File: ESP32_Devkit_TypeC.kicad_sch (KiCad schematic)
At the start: 57 parts, among them J1 USB_C_Receptacle_USB2.0, J2 Conn_01x19, J3 Conn_01x19, Q1 SS8050, Q2 SS8050, SW1 EN, SW2 BOOT, U1 MP2359, U2 CH340G, U3 ESP32-PICO-D4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

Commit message: Updated DC-DC convertor, fixed CH340G Vout
I changed switching regulator to MP2259, because MP2359 is not recommended for new designs and is therefore more futureproof.
Resistor values was also changed to lower the voltage from 3.5V to 3.33V.
I also changed USB-C type to TYPE-C-31-M-12, because I have it :) It also seems to be more popular and I saw many compatible clones on Aliexpress for example.
CH340G was set to operate with 5V signals, which isn't good for ESP, so I changed it. I also changed the part to CH340C to avoid using external crystal (which will be optional for CH340G compatibility).
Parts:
- J1: footprint Connector_USB:USB_C_Receptacle_Palconn_UTC16-G -> Connector_USB:USB_C_Receptacle_HRO_TYPE-C-31-M-12; LCSC C167321 -> C165948
- R5: value 49.9kR -> 56kR; LCSC C25897 -> C25796
- R6: value 15 kR -> 18 kR; LCSC C25756 -> C25762
- U1: value MP2359 -> MP2259; LCSC C14259 -> C82266
- U2: value CH340G -> CH340C; LCSC C14267 -> C84681
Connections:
- net +3V3: now also C5.2, C7.2, U2.16 (VCC), U2.4 (V3)
- net GND: now also C5.1; no longer C5.2
- net VBUS: no longer C7.2, U2.16 (VCC)
- no-connect marks 2 -> 9
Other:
- note added: "Populate only if CH340G is used!"
- moved on the sheet: C1, C10, C11, C2, C3, C4, C5, C7, C8, C9, D1, D2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

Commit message: Changed 4.7uF inductor part
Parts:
- L1: LCSC C86070 -> C90319
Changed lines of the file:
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@@
       (effects (font (size 1.27 1.27)) hide)
     )
-    (property "LCSC" "C86070" (id 4) (at 78.74 149.86 90)
+    (property "LCSC" " C90319" (id 4) (at 78.74 149.86 90)
       (effects (font (size 1.27 1.27)) hide)
     )

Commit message: Updated footprints, reconnected CH340C
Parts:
- J1: footprint Connector_USB:USB_C_Receptacle_HRO_TYPE-C-31-M-12 -> Moucha_Connectors:USBC_Receptacle_TYPE-C-31-M-12
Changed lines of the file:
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@@
     (property "Reference" "J1" (id 0) (at 37.0078 40.2082 0))
     (property "Value" "USB_C_Receptacle_USB2.0" (id 1) (at 37.0078 42.5196 0))
-    (property "Footprint" "Connector_USB:USB_C_Receptacle_HRO_TYPE-C-31-M-12" (id 2) (at 38.1 62.23 0)
+    (property "Footprint" "Moucha_Connectors:USBC_Receptacle_TYPE-C-31-M-12" (id 2) (at 38.1 62.23 0)
       (effects (font (size 1.27 1.27)) hide)
     )
@@
   (symbol (lib_id "power:+3V3") (at 83.82 33.02 0) (unit 1)
     (in_bom yes) (on_board yes)
-    (property "Reference" "#PWR?" (id 0) (at 83.82 36.83 0)
+    (property "Reference" "#PWR0130" (id 0) (at 83.82 36.83 0)
       (effects (font (size 1.27 1.27)) hide)
     )
@@
   (symbol (lib_id "power:GND") (at 69.85 41.91 0) (unit 1)
     (in_bom yes) (on_board yes)
-    (property "Reference" "#PWR?" (id 0) (at 69.85 48.26 0)
+    (property "Reference" "#PWR0106" (id 0) (at 69.85 48.26 0)
       (effects (font (size 1.27 1.27)) hide)
     )
@@
       (reference "#PWR0105") (unit 1) (value "GND") (footprint "")
     )
+    (path "/e89e4f7f-5566-4b18-a6b1-ab29876f8a10"
+      (reference "#PWR0106") (unit 1) (value "GND") (footprint "")
+    )
     (path "/00000000-0000-0000-0000-00005eb6312c"
       (reference "#PWR0107") (unit 1) (value "GND") (footprint "")
@@
     )
     (path "/81b97e70-46f3-4336-aebf-837d4cb8d978"
-      (reference "#PWR?") (unit 1) (value "+3V3") (footprint "")
-    )
-    (path "/e89e4f7f-5566-4b18-a6b1-ab29876f8a10"
-      (reference "#PWR?") (unit 1) (value "GND") (footprint "")
+      (reference "#PWR0130") (unit 1) (value "+3V3") (footprint "")
     )
     (path "/00000000-0000-0000-0000-00005f1a8ada"
@@
     )
     (path "/00000000-0000-0000-0000-00005eb3eb53"
-      (reference "J1") (unit 1) (value "USB_C_Receptacle_USB2.0") (footprint "Connector_USB:USB_C_Receptacle_HRO_TYPE-C-31-M-12")
+      (reference "J1") (unit 1) (value "USB_C_Receptacle_USB2.0") (footprint "Moucha_Connectors:USBC_Receptacle_TYPE-C-31-M-12")
     )
     (path "/00000000-0000-0000-0000-00005eca1541"

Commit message: Changed button type, DRC fixes
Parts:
- SW1, SW2: footprint Button_Switch_SMD:SW_Push_SPST_NO_Alps_SKRK -> Moucha_Primitives:SW_Push_1P1T_Vertical_3x4mm; LCSC C115357 -> C589212
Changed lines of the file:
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@@
     (property "Reference" "SW1" (id 0) (at 149.86 49.911 0))
     (property "Value" "EN" (id 1) (at 149.86 52.2224 0))
-    (property "Footprint" "Button_Switch_SMD:SW_Push_SPST_NO_Alps_SKRK" (id 2) (at 149.86 52.07 0)
+    (property "Footprint" "Moucha_Primitives:SW_Push_1P1T_Vertical_3x4mm" (id 2) (at 149.86 52.07 0)
       (effects (font (size 1.27 1.27)) hide)
     )
@@
       (effects (font (size 1.27 1.27)) hide)
     )
-    (property "LCSC" "C115357" (id 4) (at 149.86 57.15 0)
+    (property "LCSC" "C589212" (id 4) (at 149.86 57.15 0)
       (effects (font (size 1.27 1.27)) hide)
     )
@@
     (property "Reference" "SW2" (id 0) (at 149.86 70.231 0))
     (property "Value" "BOOT" (id 1) (at 149.86 72.5424 0))
-    (property "Footprint" "Button_Switch_SMD:SW_Push_SPST_NO_Alps_SKRK" (id 2) (at 149.86 72.39 0)
+    (property "Footprint" "Moucha_Primitives:SW_Push_1P1T_Vertical_3x4mm" (id 2) (at 149.86 72.39 0)
       (effects (font (size 1.27 1.27)) hide)
     )
@@
       (effects (font (size 1.27 1.27)) hide)
     )
-    (property "LCSC" "C115357" (id 4) (at 149.86 77.47 0)
+    (property "LCSC" "C589212" (id 4) (at 149.86 77.47 0)
       (effects (font (size 1.27 1.27)) hide)
     )
@@
     )
     (path "/00000000-0000-0000-0000-00005eca28f9"
-      (reference "SW1") (unit 1) (value "EN") (footprint "Button_Switch_SMD:SW_Push_SPST_NO_Alps_SKRK")
+      (reference "SW1") (unit 1) (value "EN") (footprint "Moucha_Primitives:SW_Push_1P1T_Vertical_3x4mm")
     )
     (path "/00000000-0000-0000-0000-00005eca6673"
-      (reference "SW2") (unit 1) (value "BOOT") (footprint "Button_Switch_SMD:SW_Push_SPST_NO_Alps_SKRK")
+      (reference "SW2") (unit 1) (value "BOOT") (footprint "Moucha_Primitives:SW_Push_1P1T_Vertical_3x4mm")
     )
     (path "/00000000-0000-0000-0000-00005eb3cfab"

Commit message: updated documentation
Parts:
- AE1, C10, C11, C9, H1, H2, I2, JP1: now left out of the parts list
- J1: footprint Moucha_Connectors:USBC_Receptacle_TYPE-C-31-M-12 -> Connector_USB:USB_C_Receptacle_HRO_TYPE-C-31-M-12
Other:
- moved on the sheet: AE1, C12, C13, C14, C15, C16, C17, C18, C19, C20, C21, C22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

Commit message: Fixed component rotation
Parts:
- L1: LCSC C90319 -> C90319
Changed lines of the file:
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@@
       (effects (font (size 1.27 1.27)) hide)
     )
-    (property "LCSC" " C90319" (id 4) (at 78.74 149.86 90)
+    (property "LCSC" "C90319" (id 4) (at 78.74 149.86 90)
       (effects (font (size 1.27 1.27)) hide)
     )

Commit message: Rev EB serial transciever bugfix, component upgrade
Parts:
- U3: footprint Package_ESP32:ESP32-Pico-D4 -> Package_ESP32:ESP32-Pico-D4-Handsolder
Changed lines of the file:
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@@
   (title_block
     (title "ESP32 DevKit Type C")
-    (date "2022-03-13")
-    (rev "F")
+    (date "2022-03-17")
+    (rev "EB")
   )
   (junction (at 60.96 99.06) (diameter 0) (color 0 0 0 0)
@@
     (stroke (width 0) (type default) (color 0 0 0 0))
   )
-  (polyline (pts (xy 50.8 77.47) (xy 80.01 77.47))
+  (polyline (pts (xy 50.8 80.01) (xy 80.01 77.47))
     (stroke (width 0) (type default) (color 0 0 0 0))
   )
@@
     (stroke (width 0) (type default) (color 0 0 0 0))
   )
-  (polyline (pts (xy 50.8 100.33) (xy 50.8 77.47))
+  (polyline (pts (xy 50.8 100.33) (xy 50.8 80.01))
     (stroke (width 0) (type default) (color 0 0 0 0))
   )
@@
     (property "Reference" "U3" (id 0) (at 208.28 78.74 0))
     (property "Value" "ESP32-PICO-D4" (id 1) (at 234.95 78.74 0))
-    (property "Footprint" "Package_ESP32:ESP32-Pico-D4" (id 2) (at 222.25 161.29 0)
+    (property "Footprint" "Package_ESP32:ESP32-Pico-D4-Handsolder" (id 2) (at 222.25 161.29 0)
       (effects (font (size 1.27 1.27)) hide)
     )
@@
     )
     (path "/00000000-0000-0000-0000-00005eb3c833"
-      (reference "U3") (unit 1) (value "ESP32-PICO-D4") (footprint "Package_ESP32:ESP32-Pico-D4")
+      (reference "U3") (unit 1) (value "ESP32-PICO-D4") (footprint "Package_ESP32:ESP32-Pico-D4-Handsolder")
     )
     (path "/00000000-0000-0000-0000-00005eb3dda3"

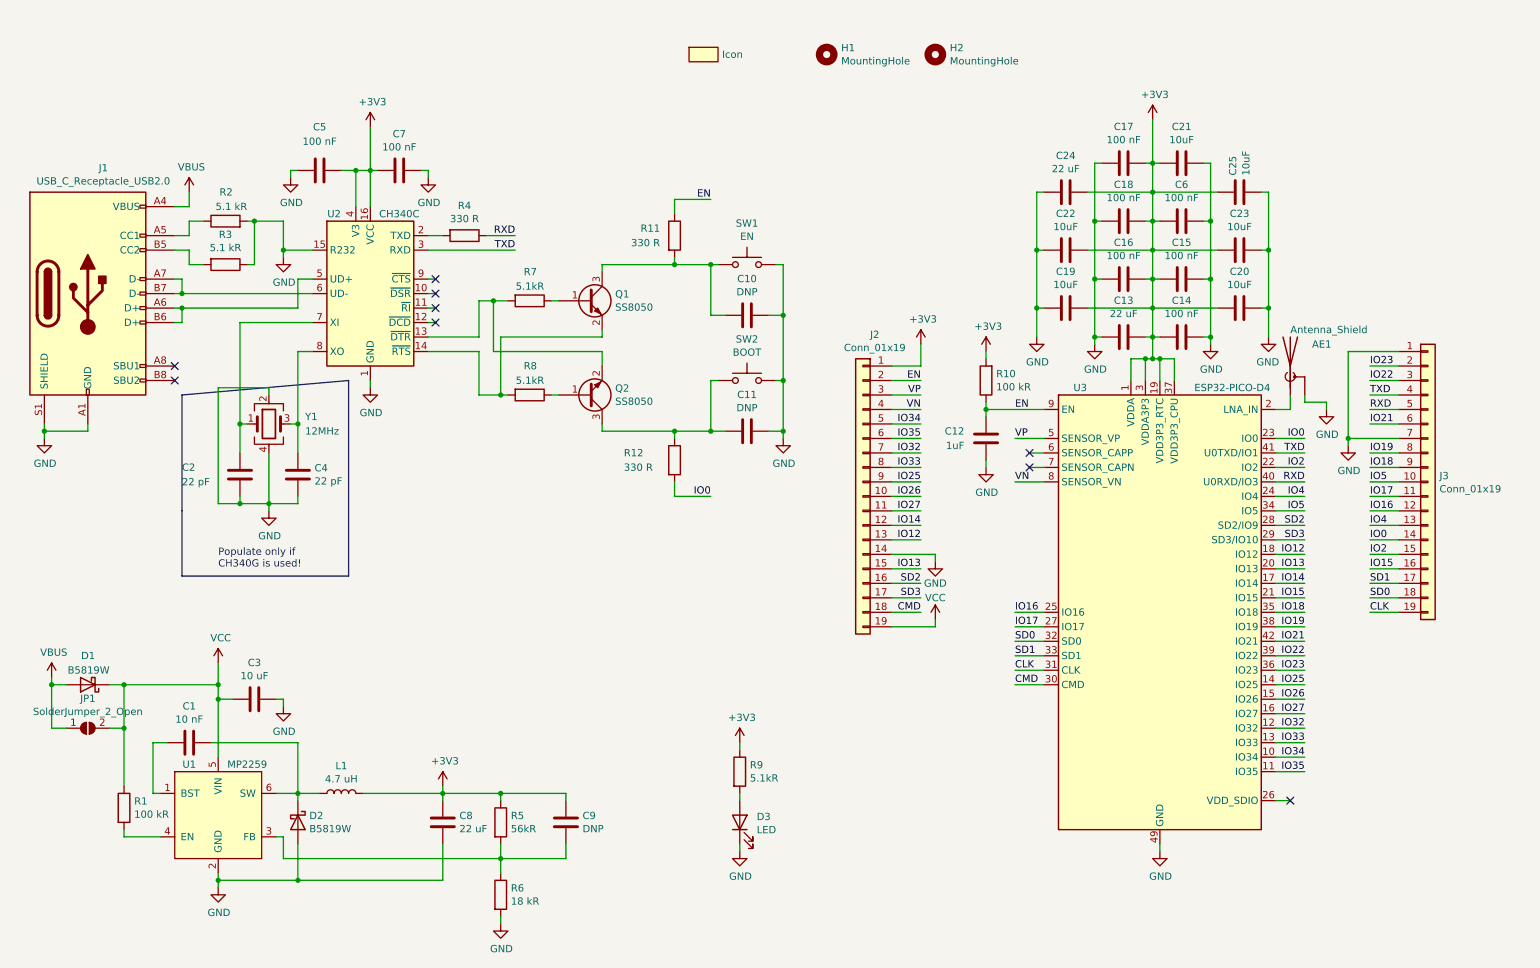
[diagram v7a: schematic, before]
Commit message: Rev EC
updated ESP32 footprint based on datasheet, minor silkscreen fixes
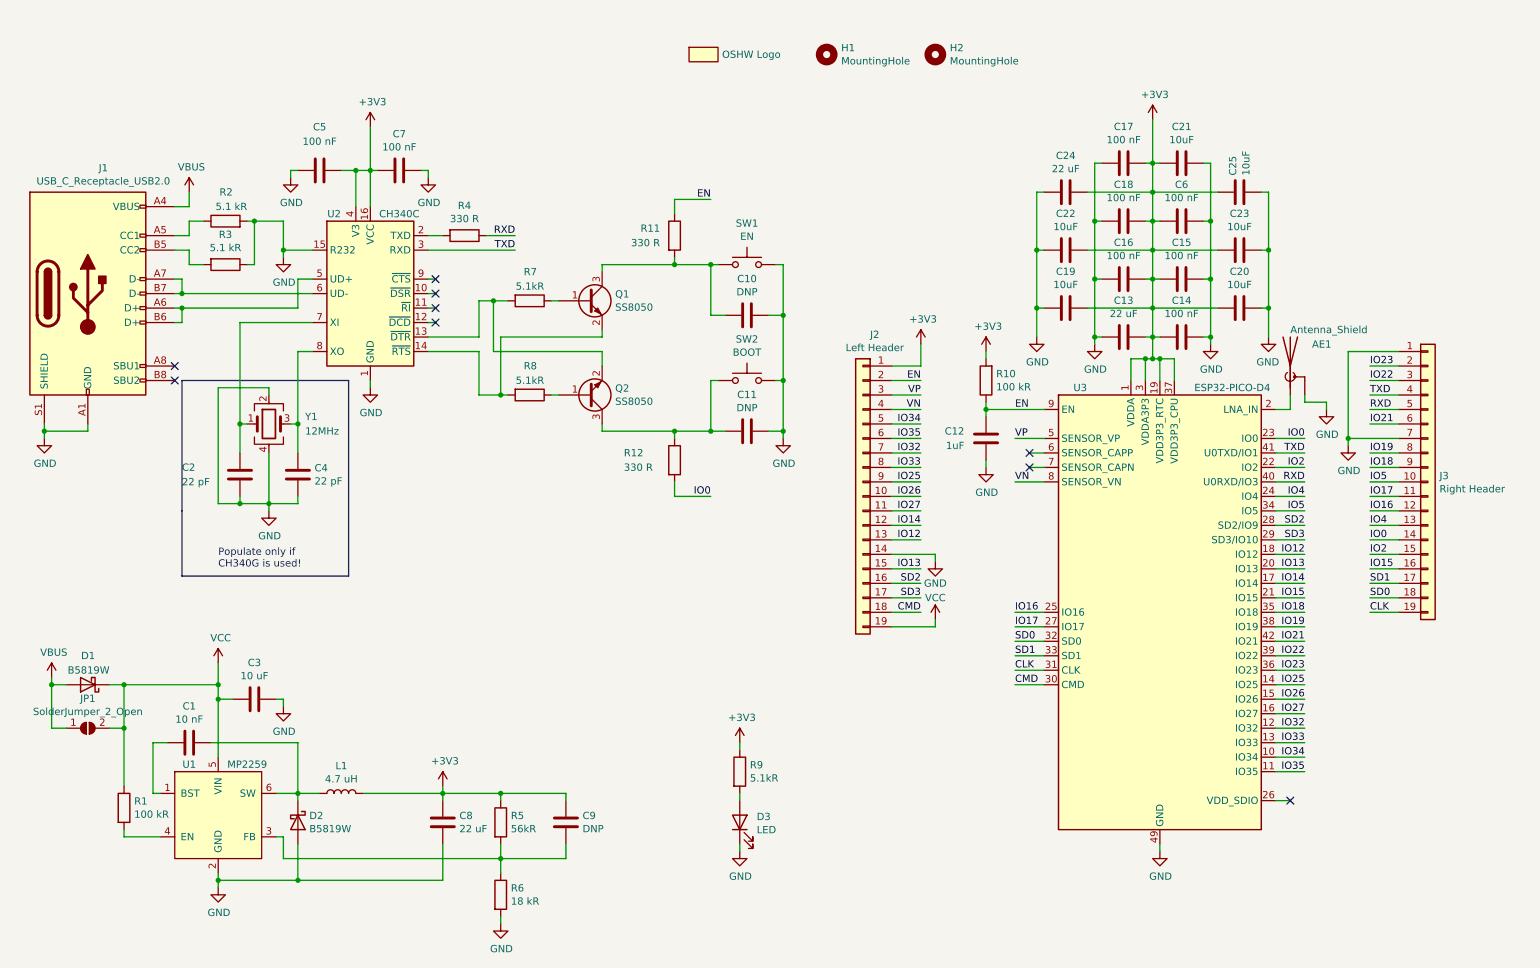
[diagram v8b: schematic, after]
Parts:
- I2: value Icon -> OSHW Logo
- J2: value Conn_01x19 -> Left Header
- J3: value Conn_01x19 -> Right Header
- U3: footprint Package_ESP32:ESP32-Pico-D4-Handsolder -> Package_ESP32:ESP32-Pico-D4-Thermal
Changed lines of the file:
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@@
   (title_block
     (title "ESP32 DevKit Type C")
-    (date "2022-03-17")
-    (rev "EB")
+    (date "2022-03-21")
+    (rev "EC")
   )
   (junction (at 60.96 99.06) (diameter 0) (color 0 0 0 0)
@@
     (stroke (width 0) (type default) (color 0 0 0 0))
   )
-  (polyline (pts (xy 50.8 80.01) (xy 80.01 77.47))
+  (polyline (pts (xy 50.8 77.47) (xy 80.01 77.47))
     (stroke (width 0) (type default) (color 0 0 0 0))
   )
@@
     (stroke (width 0) (type default) (color 0 0 0 0))
   )
-  (polyline (pts (xy 50.8 100.33) (xy 50.8 80.01))
+  (polyline (pts (xy 50.8 100.33) (xy 50.8 77.47))
     (stroke (width 0) (type default) (color 0 0 0 0))
   )
@@
     (property "Reference" "U3" (id 0) (at 208.28 78.74 0))
     (property "Value" "ESP32-PICO-D4" (id 1) (at 234.95 78.74 0))
-    (property "Footprint" "Package_ESP32:ESP32-Pico-D4-Handsolder" (id 2) (at 222.25 161.29 0)
+    (property "Footprint" "Package_ESP32:ESP32-Pico-D4-Thermal" (id 2) (at 222.25 161.29 0)
       (effects (font (size 1.27 1.27)) hide)
     )
@@
     (in_bom yes) (on_board yes)
     (property "Reference" "J2" (id 0) (at 172.2628 69.4182 0))
-    (property "Value" "Conn_01x19" (id 1) (at 172.2628 71.7296 0))
+    (property "Value" "Left Header" (id 1) (at 172.2628 71.7296 0))
     (property "Footprint" "Connector_PinHeader_2.54mm:PinHeader_1x19_P2.54mm_Vertical" (id 2) (at 170.18 97.79 0)
       (effects (font (size 1.27 1.27)) hide)
@@
       (effects (font (size 1.27 1.27)) (justify left))
     )
-    (property "Value" "Conn_01x19" (id 1) (at 271.272 96.4946 0)
+    (property "Value" "Right Header" (id 1) (at 271.272 96.4946 0)
       (effects (font (size 1.27 1.27)) (justify left))
     )
@@
       (effects (font (size 1.27 1.27)) hide)
     )
-    (property "Value" "Icon" (id 1) (at 145.4912 20.32 0)
+    (property "Value" "OSHW Logo" (id 1) (at 145.4912 20.32 0)
       (effects (font (size 1.27 1.27)) (justify left))
     )
@@
     )
     (path "/00000000-0000-0000-0000-00005f3fe9ba"
-      (reference "I2") (unit 1) (value "Icon") (footprint "Signs:OSHW_icon_3.3x3")
+      (reference "I2") (unit 1) (value "OSHW Logo") (footprint "Signs:OSHW_icon_3.3x3")
     )
     (path "/00000000-0000-0000-0000-00005eb3eb53"
@@
     )
     (path "/00000000-0000-0000-0000-00005eca1541"
-      (reference "J2") (unit 1) (value "Conn_01x19") (footprint "Connector_PinHeader_2.54mm:PinHeader_1x19_P2.54mm_Vertical")
+      (reference "J2") (unit 1) (value "Left Header") (footprint "Connector_PinHeader_2.54mm:PinHeader_1x19_P2.54mm_Vertical")
     )
     (path "/00000000-0000-0000-0000-00005ed12cc6"
-      (reference "J3") (unit 1) (value "Conn_01x19") (footprint "Connector_PinHeader_2.54mm:PinHeader_1x19_P2.54mm_Vertical")
+      (reference "J3") (unit 1) (value "Right Header") (footprint "Connector_PinHeader_2.54mm:PinHeader_1x19_P2.54mm_Vertical")
     )
     (path "/00000000-0000-0000-0000-00005f7702d8"
@@
     )
     (path "/00000000-0000-0000-0000-00005eb3c833"
-      (reference "U3") (unit 1) (value "ESP32-PICO-D4") (footprint "Package_ESP32:ESP32-Pico-D4-Handsolder")
+      (reference "U3") (unit 1) (value "ESP32-PICO-D4") (footprint "Package_ESP32:ESP32-Pico-D4-Thermal")
     )
     (path "/00000000-0000-0000-0000-00005eb3dda3"
